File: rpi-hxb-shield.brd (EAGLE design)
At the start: 44 x 40.5 mm, 22 parts, among them Q1 CRYSTALX22, U2 24LC128-I/SN

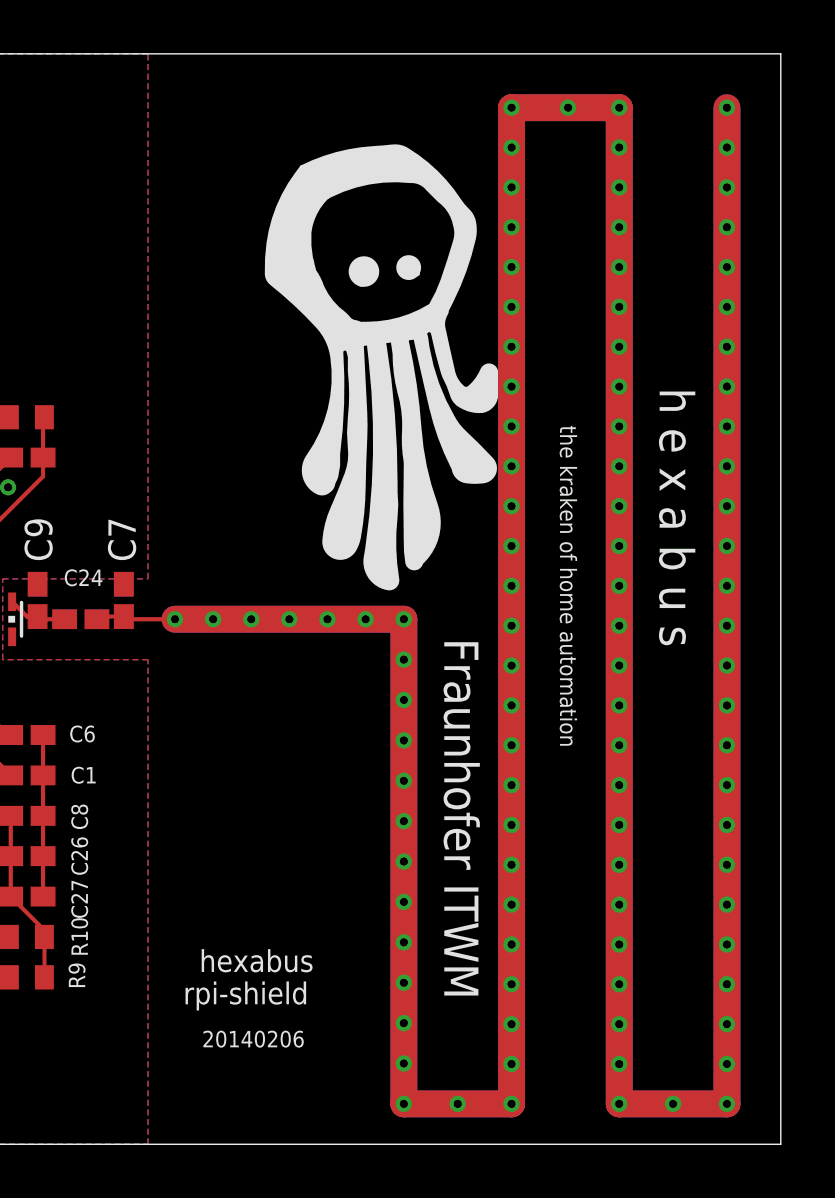
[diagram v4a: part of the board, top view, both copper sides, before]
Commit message: fixed overlap issue
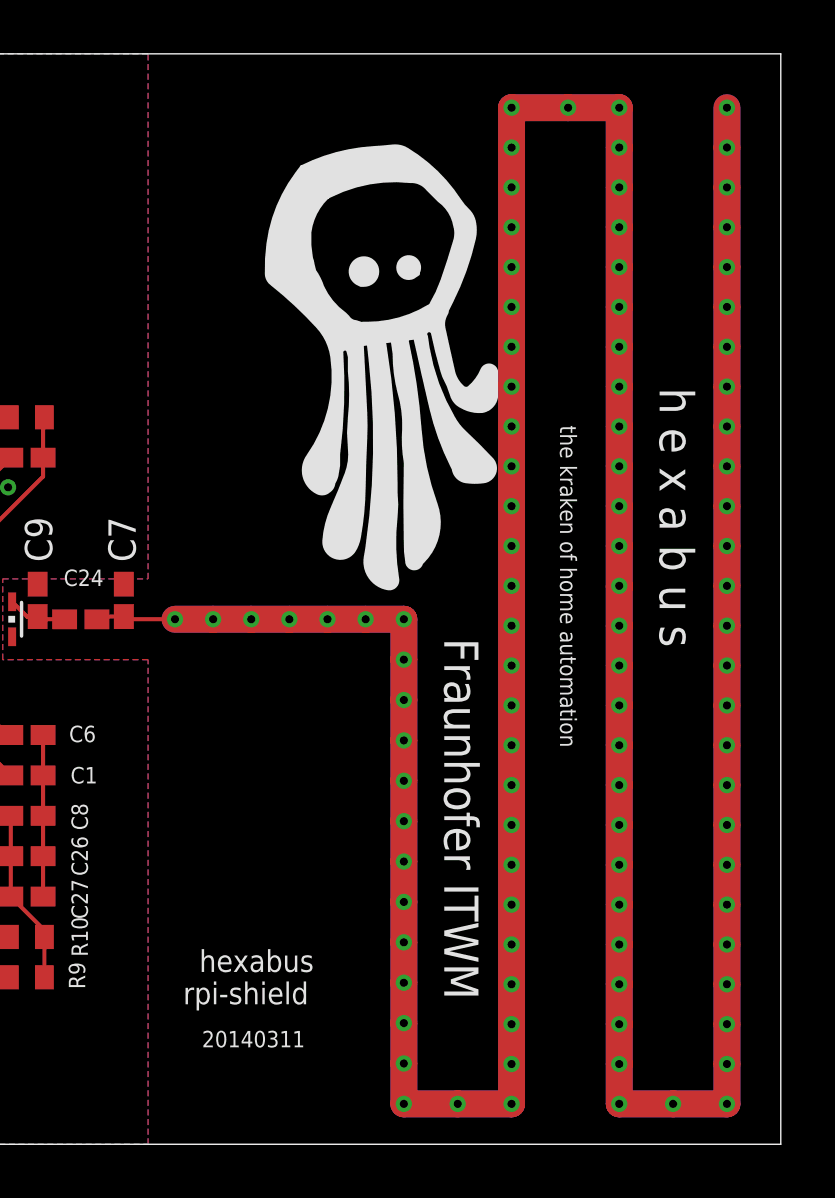
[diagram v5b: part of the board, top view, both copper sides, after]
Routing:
- net ANTENNA: track 302.0 -> 305.1 mm, vias 25 -> 100
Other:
- board text added: "20140311"
- board text removed: "20140206"
